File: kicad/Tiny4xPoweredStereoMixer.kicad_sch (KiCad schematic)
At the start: 23 parts, among them J1 RCJ-2221, J2 RCJ-2221, J3 RCJ-2221, J4 RCJ-2221, J5 RCJ-2221, J6 PowerConnector, J7 PowerConnector, J8 PowerConnector, U6 LM2611AMF/NOPB

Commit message: -  Fixed in-rush current problem using soft-start design. https://github.com/cracked-machine/Tiny4xPoweredStereoMixer/issues/4 - Fixed reversed pots. https://github.com/cracked-machine/Tiny4xPoweredStereoMixer/issues/3 - Made more space surrounding pwr in connector. https://github.com/cracked-machine/Tiny4xPoweredStereoMixer/issues/8
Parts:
- added C16: 100nF, Capacitor_SMD:C_0603_1608Metric_Pad1.08x0.95mm_HandSolder, symbol Device:C
- added R11: 100k, Resistor_SMD:R_0805_2012Metric_Pad1.20x1.40mm_HandSolder, symbol Device:R
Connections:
- net at C3.2, C4.2, J8.1 (Pin_1)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: now also C16.1
- net at C1.2, C15.1, J6.2 (Pin_2)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: now also R11.1; no longer U6.4 (~{SHDN})
- new net: C16.2, R11.2, U6.4 (~{SHDN})
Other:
- note added: "AUDIO PATH"
- note added: "CUK SMPS"
- moved on the sheet: C1, C15, C2, C3, C4, D1, H1, H2, H3, H4, J1, J2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

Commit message: Refactored schematic into single page (except PSU)
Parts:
- removed C1, C4: 22u, Capacitor_SMD:C_1210_3225Metric_Pad1.33x2.70mm_HandSolder, symbol Device:C
- removed C15, C16: 100nF, Capacitor_SMD:C_0603_1608Metric_Pad1.08x0.95mm_HandSolder, symbol Device:C
- removed C2: 2.2u, Capacitor_SMD:C_1210_3225Metric_Pad1.33x2.70mm_HandSolder, symbol Device:C
- removed C3: 1n, Capacitor_SMD:C_0805_2012Metric_Pad1.18x1.45mm_HandSolder, symbol Device:C
- removed D1: D_Schottky, Diode_SMD:D_PowerDI-123, symbol Device:D_Schottky
- removed J6, J7, J8: PowerConnector, Connector_PinHeader_2.54mm:PinHeader_1x02_P2.54mm_Vertical, symbol Connector:Conn_01x02_Pin
- removed L1, L2: 22u, Inductor_SMD:L_Ferrocore_DLG-0403, symbol Device:L
- removed R11: 100k, Resistor_SMD:R_0805_2012Metric_Pad1.20x1.40mm_HandSolder, symbol Device:R
- removed RFB1: 22k, Resistor_SMD:R_0805_2012Metric_Pad1.20x1.40mm_HandSolder, symbol Device:R
- removed RFB2: 2k2, Resistor_SMD:R_0805_2012Metric_Pad1.20x1.40mm_HandSolder, symbol Device:R
- removed U6: LM2611AMF/NOPB, Package_TO_SOT_SMD:SOT-23-5, symbol Regulator_Switching:LM2611xMF
- added C10, C11, C12, C13, C14, C5, C6, C7, C8, C9: 100nF, Capacitor_SMD:C_0603_1608Metric_Pad1.08x0.95mm_HandSolder, symbol Device:C
- added R1, R10, R2, R3, R4, R5, R6, R7, R8, R9: 10k, Resistor_SMD:R_0805_2012Metric_Pad1.20x1.40mm_HandSolder, symbol Device:R
- added RV1, RV2, RV3, RV4: 10k, Potentiometers:Potentiometer_Alps_RK09L_Double_Horizontal, symbol Device:R_Potentiometer_Dual_Separate
- added U1, U2, U3, U4, U5: TL072, Package_SO:SOIC-8_3.9x4.9mm_P1.27mm, symbol Amplifier_Operational:TL072
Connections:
- net +12V: now also C11.1, C13.1, C5.1, C7.1, C9.1, U1.8 (V+), U2.8 (V+), U3.8 (V+), U4.8 (V+), U5.8 (V+)
- net -12V: now also C10.1, C12.1, C14.1, C6.1, C8.1, U1.4 (V-), U2.4 (V-), U3.4 (V-), U4.4 (V-), U5.4 (V-)
- net GND: now also C10.2, C11.2, C12.2, C13.2, C14.2, C5.2, C6.2, C7.2, C8.2, C9.2, RV1.1, RV1.4, RV2.1, RV2.4, RV3.1, RV3.4, RV4.1, RV4.4, U5.3 (+), U5.5 (+)
- net BufferOpAmp1/left_channel_input: no longer names the net of J1.3 (Pin_3)
- net BufferOpAmp1/left_channel_input: now also U1.3 (+)
- net BufferOpAmp1/right_channel_input: no longer names the net of J1.2 (Pin_2)
- net BufferOpAmp1/right_channel_input: now also U1.5 (+)
- net BufferOpAmp2/left_channel_input: no longer names the net of J2.3 (Pin_3)
- net BufferOpAmp2/left_channel_input: now also U2.3 (+)
- net BufferOpAmp2/right_channel_input: no longer names the net of J2.2 (Pin_2)
- net BufferOpAmp2/right_channel_input: now also U2.5 (+)
- net BufferOpAmp3/left_channel_input: no longer names the net of J3.3 (Pin_3)
- net BufferOpAmp3/left_channel_input: now also U3.3 (+)
- net BufferOpAmp3/right_channel_input: no longer names the net of J3.2 (Pin_2)
- net BufferOpAmp3/right_channel_input: now also U3.5 (+)
- net BufferOpAmp4/left_channel_input: no longer names the net of J4.3 (Pin_3)
- net BufferOpAmp4/left_channel_input: now also U4.3 (+)
- net BufferOpAmp4/right_channel_input: no longer names the net of J4.2 (Pin_2)
- net BufferOpAmp4/right_channel_input: now also U4.5 (+)
- net MixerOpAmp/left_channel_mix_out: no longer names the net of J5.3 (Pin_3)
- net MixerOpAmp/left_channel_mix_out: now also R9.2, U5.1
- net MixerOpAmp/right_channel_mix_out: no longer names the net of J5.2 (Pin_2)
- net MixerOpAmp/right_channel_mix_out: now also R10.2, U5.7
- new net: RV3.3, U3.6 (-), U3.7
- new net: RV3.6, U3.1, U3.2 (-)
- new net: R10.1, R5.2, R6.2, R7.2, R8.2, U5.6 (-)
- new net: R1.2, R2.2, R3.2, R4.2, R9.1, U5.2 (-)
- new net: RV1.3, U1.6 (-), U1.7
- new net: RV2.3, U2.6 (-), U2.7
- new net: RV4.3, U4.6 (-), U4.7
- new net: RV1.6, U1.1, U1.2 (-)
- new net: RV4.6, U4.1, U4.2 (-)
- new net: RV2.6, U2.1, U2.2 (-)
- new net ch1_left_mix_in: R4.1, RV1.5
- new net ch1_right_mix_in: R8.1, RV1.2
- new net ch2_left_mix_in: R3.1, RV2.5
- new net ch2_right_mix_in: R7.1, RV2.2
- new net ch3_left_mix_in: R2.1, RV3.5
- new net ch3_right_mix_in: R6.1, RV3.2
- new net ch4_left_mix_in: R1.1, RV4.5
- new net ch4_right_mix_in: R5.1, RV4.2
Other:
- removed sheet BufferOpAmp1
- removed sheet BufferOpAmp2
- removed sheet BufferOpAmp3
- removed sheet BufferOpAmp4
- removed sheet MixerOpAmp
- added sheet PowerSupply (PowerSupply.kicad_sch)
- note removed: "AUDIO PATH"
- note removed: "CUK SMPS"
- moved on the sheet: H1, H2, H3, H4, J1, J5

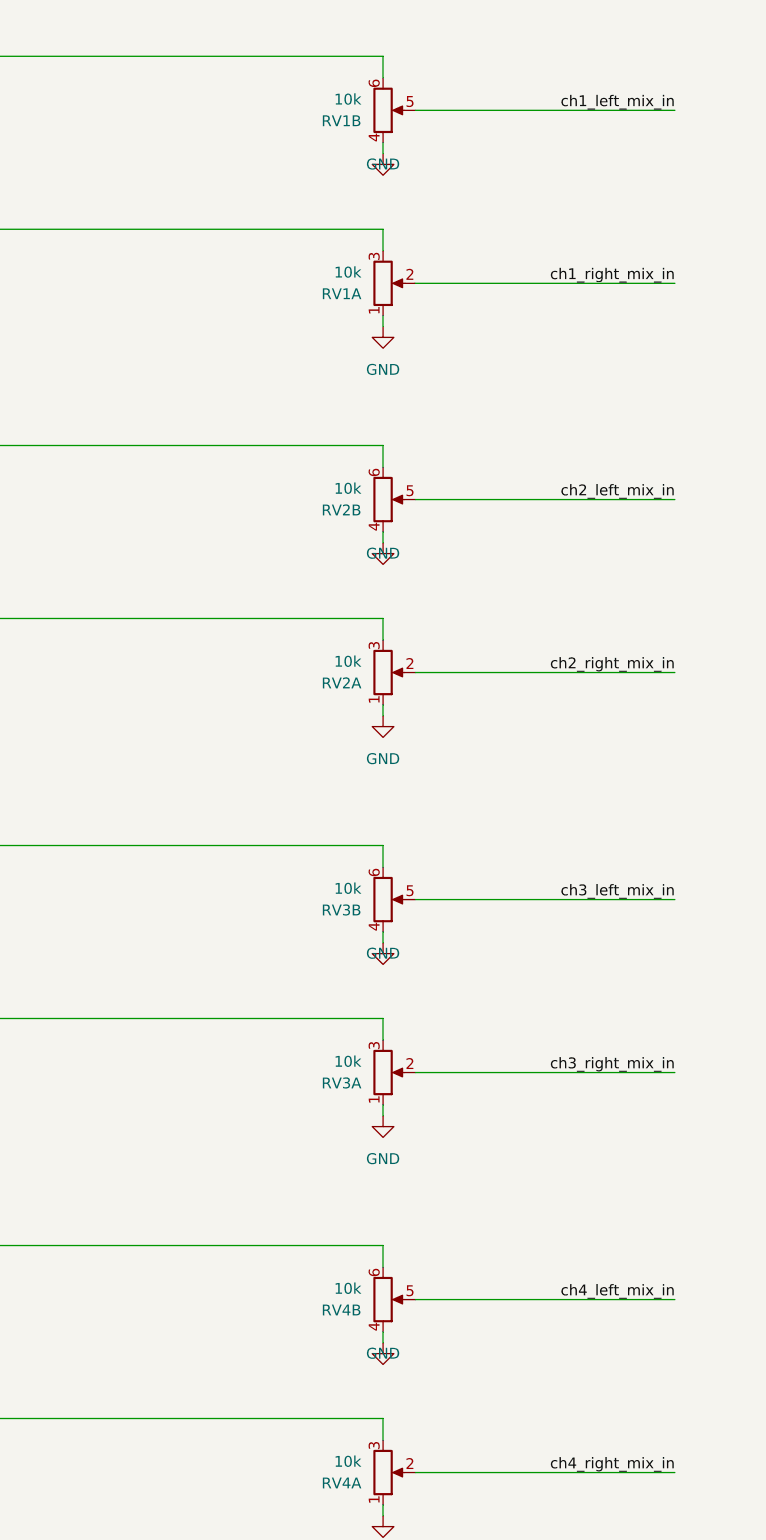
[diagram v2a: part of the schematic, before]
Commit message: - updated pots to rk12l12
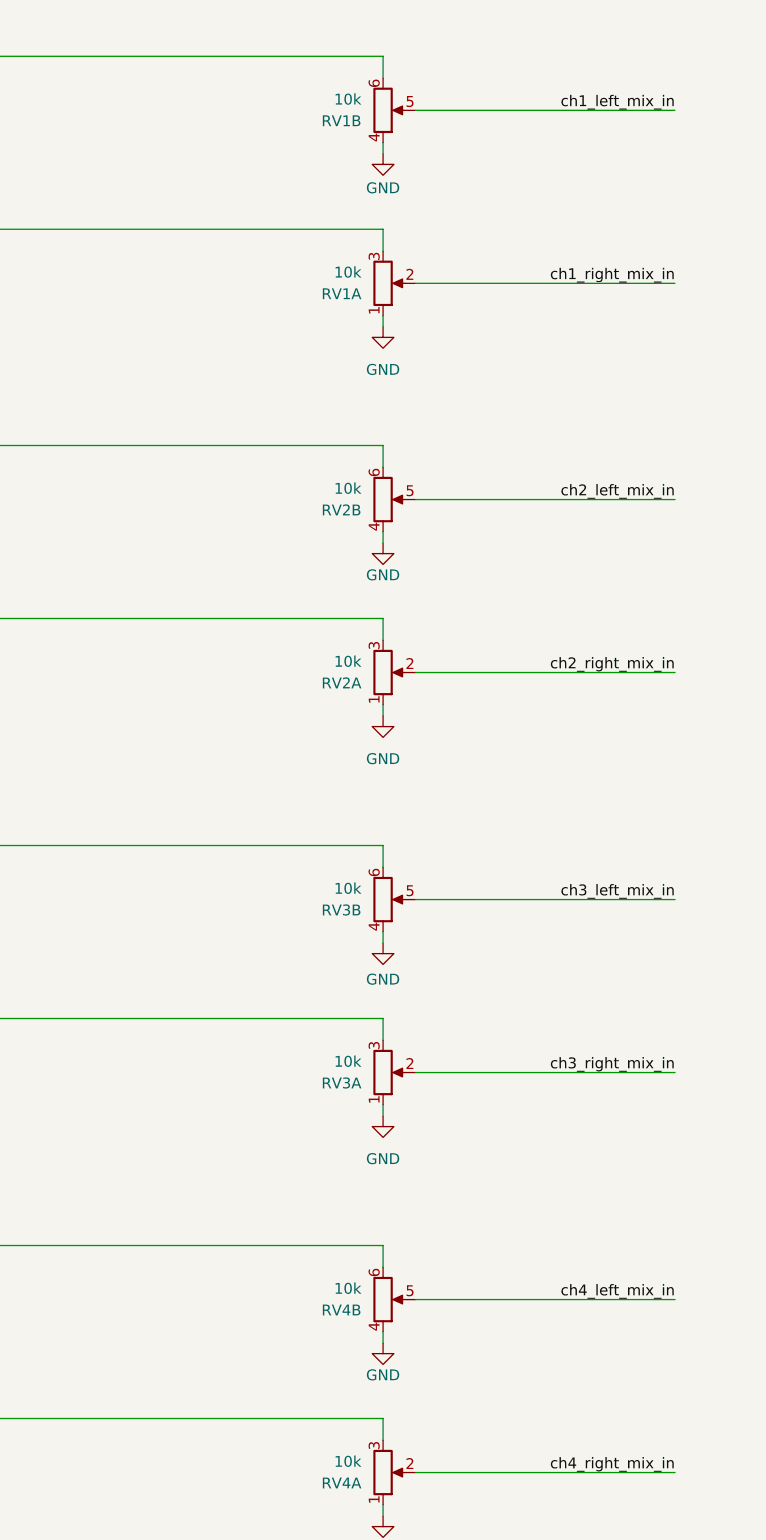
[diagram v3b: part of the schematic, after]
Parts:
- RV1, RV2, RV3, RV4: footprint Potentiometers:Potentiometer_Alps_RK09L_Double_Horizontal -> Potentiometers:Alps_RK12L12_Double_Horizontal; Mouser 688-RK09L12B0A4S -> 688-RK12L1210C1K
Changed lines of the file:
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@@
 			)
 		)
-		(property "Footprint" "Potentiometers:Potentiometer_Alps_RK09L_Double_Horizontal"
+		(property "Footprint" "Potentiometers:Alps_RK12L12_Double_Horizontal"
 			(at 160.02 57.15 0)
 			(effects
@@
 			)
 		)
-		(property "Datasheet" "~"
+		(property "Datasheet" "https://www.mouser.co.uk/datasheet/2/15/RK12L12_VARIETYOTHER-1370614.pdf"
 			(at 160.02 57.15 0)
 			(effects
@@
 			)
 		)
-		(property "Description" "Dual potentiometer, separate units"
+		(property "Description" "Dual potentiometer, separate units, linear taper"
 			(at 160.02 57.15 0)
 			(effects
@@
 			)
 		)
-		(property "Mouser" "688-RK09L12B0A4S "
+		(property "Mouser" "688-RK12L1210C1K "
 			(at 160.02 57.15 0)
 			(effects
@@
 			)
 		)
-		(property "Footprint" "Potentiometers:Potentiometer_Alps_RK09L_Double_Horizontal"
+		(property "Footprint" "Potentiometers:Alps_RK12L12_Double_Horizontal"
 			(at 160.02 102.87 0)
 			(effects
@@
 			)
 		)
-		(property "Datasheet" "~"
+		(property "Datasheet" "https://www.mouser.co.uk/datasheet/2/15/RK12L12_VARIETYOTHER-1370614.pdf"
 			(at 160.02 102.87 0)
 			(effects
@@
 			)
 		)
-		(property "Description" "Dual potentiometer, separate units"
+		(property "Description" "Dual potentiometer, separate units, linear taper"
 			(at 160.02 102.87 0)
 			(effects
@@
 			)
 		)
-		(property "Mouser" "688-RK09L12B0A4S "
+		(property "Mouser" "688-RK12L1210C1K "
 			(at 160.02 102.87 0)
 			(effects
@@
 			)
 		)
-		(property "Datasheet" "~"
+		(property "Datasheet" "https://www.mouser.co.uk/datasheet/2/670/rcj_22-3159382.pdf"
 			(at 41.91 132.08 0)
 			(effects
@@
 			)
 		)
-		(property "Footprint" "Potentiometers:Potentiometer_Alps_RK09L_Double_Horizontal"
+		(property "Footprint" "Potentiometers:Alps_RK12L12_Double_Horizontal"
 			(at 160.02 196.85 0)
 			(effects
@@
 			)
 		)
-		(property "Datasheet" "~"
+		(property "Datasheet" "https://www.mouser.co.uk/datasheet/2/15/RK12L12_VARIETYOTHER-1370614.pdf"
 			(at 160.02 196.85 0)
 			(effects
@@
 			)
 		)
-		(property "Description" "Dual potentiometer, separate units"
+		(property "Description" "Dual potentiometer, separate units, linear taper"
 			(at 160.02 196.85 0)
 			(effects
@@
 			)
 		)
-		(property "Mouser" "688-RK09L12B0A4S "
+		(property "Mouser" "688-RK12L1210C1K "
 			(at 160.02 196.85 0)
 			(effects
@@
 			)
 		)
-		(property "Footprint" "Potentiometers:Potentiometer_Alps_RK09L_Double_Horizontal"
+		(property "Footprint" "Potentiometers:Alps_RK12L12_Double_Horizontal"
 			(at 160.02 36.83 0)
 			(effects
@@
 			)
 		)
-		(property "Datasheet" "~"
+		(property "Datasheet" "https://www.mouser.co.uk/datasheet/2/15/RK12L12_VARIETYOTHER-1370614.pdf"
 			(at 160.02 36.83 0)
 			(effects
@@
 			)
 		)
-		(property "Description" "Dual potentiometer, separate units"
+		(property "Description" "Dual potentiometer, separate units, linear taper"
 			(at 160.02 36.83 0)
 			(effects
@@
 			)
 		)
-		(property "Mouser" "688-RK09L12B0A4S "
+		(property "Mouser" "688-RK12L1210C1K "
 			(at 160.02 36.83 0)
 			(effects
@@
 		)
 		(property "Value" "GND"
-			(at 160.02 88.9 0)
+			(at 160.02 91.44 0)
 			(effects
 				(font
@@
 			)
 		)
-		(property "Footprint" "Potentiometers:Potentiometer_Alps_RK09L_Double_Horizontal"
+		(property "Footprint" "Potentiometers:Alps_RK12L12_Double_Horizontal"
 			(at 160.02 176.53 0)
 			(effects
@@
 			)
 		)
-		(property "Datasheet" "~"
+		(property "Datasheet" "https://www.mouser.co.uk/datasheet/2/15/RK12L12_VARIETYOTHER-1370614.pdf"
 			(at 160.02 176.53 0)
 			(effects
@@
 			)
 		)
-		(property "Description" "Dual potentiometer, separate units"
+		(property "Description" "Dual potentiometer, separate units, linear taper"
 			(at 160.02 176.53 0)
 			(effects
@@
 			)
 		)
-		(property "Mouser" "688-RK09L12B0A4S "
+		(property "Mouser" "688-RK12L1210C1K "
 			(at 160.02 176.53 0)
 			(effects
@@
 		)
 		(property "Value" "GND"
-			(at 160.02 43.18 0)
+			(at 160.02 45.974 0)
 			(effects
 				(font
@@
 			)
 		)
-		(property "Footprint" "Potentiometers:Potentiometer_Alps_RK09L_Double_Horizontal"
+		(property "Footprint" "Potentiometers:Alps_RK12L12_Double_Horizontal"
 			(at 160.02 149.86 0)
 			(effects
@@
 			)
 		)
-		(property "Datasheet" "~"
+		(property "Datasheet" "https://www.mouser.co.uk/datasheet/2/15/RK12L12_VARIETYOTHER-1370614.pdf"
 			(at 160.02 149.86 0)
 			(effects
@@
 			)
 		)
-		(property "Description" "Dual potentiometer, separate units"
+		(property "Description" "Dual potentiometer, separate units, linear taper"
 			(at 160.02 149.86 0)
 			(effects
@@
 			)
 		)
-		(property "Mouser" "688-RK09L12B0A4S "
+		(property "Mouser" "688-RK12L1210C1K "
 			(at 160.02 149.86 0)
 			(effects
@@
 			)
 		)
-		(property "Footprint" "Potentiometers:Potentiometer_Alps_RK09L_Double_Horizontal"
+		(property "Footprint" "Potentiometers:Alps_RK12L12_Double_Horizontal"
 			(at 160.02 129.54 0)
 			(effects
@@
 			)
 		)
-		(property "Datasheet" "~"
+		(property "Datasheet" "https://www.mouser.co.uk/datasheet/2/15/RK12L12_VARIETYOTHER-1370614.pdf"
 			(at 160.02 129.54 0)
 			(effects
@@
 			)
 		)
-		(property "Description" "Dual potentiometer, separate units"
+		(property "Description" "Dual potentiometer, separate units, linear taper"
 			(at 160.02 129.54 0)
 			(effects
@@
 			)
 		)
-		(property "Mouser" "688-RK09L12B0A4S "
+		(property "Mouser" "688-RK12L1210C1K "
 			(at 160.02 129.54 0)
 			(effects
@@
 			)
 		)
-		(property "Footprint" "Potentiometers:Potentiometer_Alps_RK09L_Double_Horizontal"
+		(property "Footprint" "Potentiometers:Alps_RK12L12_Double_Horizontal"
 			(at 160.02 82.55 0)
 			(effects
@@
 			)
 		)
-		(property "Datasheet" "~"
+		(property "Datasheet" "https://www.mouser.co.uk/datasheet/2/15/RK12L12_VARIETYOTHER-1370614.pdf"
 			(at 160.02 82.55 0)
 			(effects
@@
 			)
 		)
-		(property "Description" "Dual potentiometer, separate units"
+		(property "Description" "Dual potentiometer, separate units, linear taper"
 			(at 160.02 82.55 0)
 			(effects
@@
 			)
 		)
-		(property "Mouser" "688-RK09L12B0A4S "
+		(property "Mouser" "688-RK12L1210C1K "
 			(at 160.02 82.55 0)
 			(effects
@@
 			)
 		)
-		(property "Datasheet" "~"
+		(property "Datasheet" "https://www.mouser.co.uk/datasheet/2/670/rcj_22-3159382.pdf"
 			(at 388.62 146.05 0)
 			(effects
@@
 			)
 		)
-		(property "Datasheet" "~"
+		(property "Datasheet" "https://www.mouser.co.uk/datasheet/2/670/rcj_22-3159382.pdf"
 			(at 41.91 85.09 0)
 			(effects
@@
 			)
 		)
-		(property "Datasheet" "~"
+		(property "Datasheet" "https://www.mouser.co.uk/datasheet/2/670/rcj_22-3159382.pdf"
 			(at 41.91 39.37 0)
 			(effects
@@
 			)
 		)
-		(property "Datasheet" "~"
+		(property "Datasheet" "https://www.mouser.co.uk/datasheet/2/670/rcj_22-3159382.pdf"
 			(at 41.91 179.07 0)
 			(effects
@@
 		)
 		(property "Value" "GND"
-			(at 160.02 135.89 0)
+			(at 160.02 138.938 0)
 			(effects
 				(font
@@
 		)
 		(property "Value" "GND"
-			(at 160.02 182.88 0)
+			(at 160.02 185.42 0)
 			(effects
 				(font

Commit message: replaced phono connectors with 3.5mm stereo jack connectors so that unplugged connections are switched to ground
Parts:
- removed H3, H4: MountingHole, MountingHole:MountingHole_3mm, symbol Mechanical:MountingHole
- removed J1, J2, J3, J4, J5: RCJ-2221, RCAJack:CUI_DEVICES_RCJ-2211, symbol Connector:Conn_01x03_Pin
- removed unit 1 of U1
- removed unit 2 of U1
- removed U3, U4: TL072, Package_SO:SOIC-8_3.9x4.9mm_P1.27mm, symbol Amplifier_Operational:TL072
- removed unit 3 of U5
- added C17, C18: 100nF, Capacitor_SMD:C_0603_1608Metric_Pad1.08x0.95mm_HandSolder, symbol Device:C
- added C19, C20: 10uF, Capacitor_SMD:C_1210_3225Metric_Pad1.33x2.70mm_HandSolder, symbol Device:C
- added J1, J2, J3, J4, J9: AudioJack3_SwitchTR, Connector_Audio:Jack_3.5mm_CUI_SJ1-3535NG_Horizontal, symbol Connector_Audio:AudioJack3_SwitchTR
- added R12, R13, R14, R15: 10k, Resistor_SMD:R_0805_2012Metric_Pad1.20x1.40mm_HandSolder, symbol Device:R
- renumbered U5 to U1
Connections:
- net +12V: no longer C11.1, C5.1, C7.1
- net -12V: no longer C10.1, C12.1, C14.1
- net GND: now also U2.3 (+), U2.5 (+), J1.RN, J1.S, J1.TN, J2.RN, J2.S, J2.TN, J3.RN, J3.S, J3.TN, J4.RN, J4.S, J4.TN, J9.RN, J9.S, J9.TN; no longer C10.2, C11.2, C12.2, C14.2, C5.2, C7.2
- net at RV3.3: now also C14.2
- net at RV3.6: now also C12.2
- net at R5.2, R6.2, R7.2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: now also R9.1, U1.2 (-); no longer R10.1, U1.6 (-)
- net at R10.2, U1.7: now also C20.1
- net at R1.2, R2.2, R3.2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: now also U2.2 (-), R13.1; no longer R9.1, U1.2 (-)
- net at RV1.3: now also C7.2
- net at R9.2, U1.1: now also R12.1
- net at RV4.3: now also C18.2
- net at RV1.6: now also C5.2
- net at RV4.6: now also C17.2
- new net: C10.1, J2.T
- new net: C10.2, RV2.6
- new net: R10.1, R12.2, U1.6 (-)
- new net: R13.2, R14.1, U2.1
- new net: R14.2, R15.1, U2.6 (-)
- new net: C18.1, J4.R
- new net: C17.1, J4.T
- new net: C19.1, R15.2, U2.7
- new net: C19.2, J9.T
- new net: C11.2, RV2.3
- new net: C7.1, J1.R
- new net: C12.1, J3.T
- new net: C14.1, J3.R
- new net: C20.2, J9.R
- new net: C5.1, J1.T
- new net: C11.1, J2.R
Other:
- moved on the sheet: R1, R10, R2, R3, R4, R5, R6, R7, R8, R9, RV1A, RV1B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

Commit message: completed revb layout
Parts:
- added TP1: TestPoint, TestPoint:TestPoint_Keystone_5005-5009_Compact, symbol Connector:TestPoint
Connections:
- net GND: now also TP1.1
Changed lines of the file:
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@@
 	(wire
 		(pts
+			(xy 83.82 256.54) (xy 83.82 260.35)
+		)
+		(stroke
+			(width 0)
+			(type default)
+		)
+	)
+	(wire
+		(pts
 			(xy 104.14 151.13) (xy 104.14 152.4)
 		)
@@
 	)
 	(symbol
+		(lib_id "power:GND")
+		(at 83.82 260.35 0)
+		(unit 1)
+		(exclude_from_sim no)
+		(in_bom yes)
+		(on_board yes)
+		(dnp no)
+		(fields_autoplaced yes)
+		(property "Reference" "#PWR08"
+			(at 83.82 266.7 0)
+			(effects
+				(font
+					(size 1.27 1.27)
+				)
+				(hide yes)
+			)
+		)
+		(property "Value" "GND"
+			(at 83.82 265.43 0)
+			(effects
+				(font
+					(size 1.27 1.27)
+				)
+			)
+		)
+		(property "Footprint" ""
+			(at 83.82 260.35 0)
+			(effects
+				(font
+					(size 1.27 1.27)
+				)
+				(hide yes)
+			)
+		)
+		(property "Datasheet" ""
+			(at 83.82 260.35 0)
+			(effects
+				(font
+					(size 1.27 1.27)
+				)
+				(hide yes)
+			)
+		)
+		(property "Description" "Power symbol creates a global label with name \"GND\" , ground"
+			(at 83.82 260.35 0)
+			(effects
+				(font
+					(size 1.27 1.27)
+				)
+				(hide yes)
+			)
+		)
+		(pin "1"
+		)
+		(instances
+			(project "Tiny4xPoweredStereoMixer"
+				(path "/68c4b081-ef47-4ba5-a55f-4ef66cb2b598"
+					(reference "#PWR08")
+					(unit 1)
+				)
+			)
+		)
+	)
+	(symbol
 		(lib_id "Device:C")
 		(at 148.59 252.73 0)
@@
 	)
 	(symbol
+		(lib_id "Connector:TestPoint")
+		(at 83.82 256.54 0)
+		(unit 1)
+		(exclude_from_sim no)
+		(in_bom yes)
+		(on_board yes)
+		(dnp no)
+		(fields_autoplaced yes)
+		(property "Reference" "TP1"
+			(at 86.36 251.9679 0)
+			(effects
+				(font
+					(size 1.27 1.27)
+				)
+				(justify left)
+			)
+		)
+		(property "Value" "TestPoint"
+			(at 86.36 254.5079 0)
+			(effects
+				(font
+					(size 1.27 1.27)
+				)
+				(justify left)
+			)
+		)
+		(property "Footprint" "TestPoint:TestPoint_Keystone_5005-5009_Compact"
+			(at 88.9 256.54 0)
+			(effects
+				(font
+					(size 1.27 1.27)
+				)
+				(hide yes)
+			)
+		)
+		(property "Datasheet" "https://www.mouser.co.uk/datasheet/2/215/5005_5009-743680.pdf"
+			(at 88.9 256.54 0)
+			(effects
+				(font
+					(size 1.27 1.27)
+				)
+				(hide yes)
+			)
+		)
+		(property "Description" "test point"
+			(at 83.82 256.54 0)
+			(effects
+				(font
+					(size 1.27 1.27)
+				)
+				(hide yes)
+			)
+		)
+		(property "Mouser" "534-5006"
+			(at 83.82 256.54 0)
+			(effects
+				(font
+					(size 1.27 1.27)
+				)
+				(hide yes)
+			)
+		)
+		(pin "1"
+		)
+		(instances
+			(project "Tiny4xPoweredStereoMixer"
+				(path "/68c4b081-ef47-4ba5-a55f-4ef66cb2b598"
+					(reference "TP1")
+					(unit 1)
+				)
+			)
+		)
+	)
+	(symbol
 		(lib_id "power:-12V")
 		(at 158.75 242.57 0)
@@
 	)
 	(sheet
-		(at 307.34 218.44)
+		(at 295.91 201.93)
 		(size 63.5 29.21)
 		(fields_autoplaced yes)
@@
 		)
 		(property "Sheetname" "PowerSupply"
-			(at 307.34 217.7284 0)
+			(at 295.91 201.2184 0)
 			(effects
 				(font
@@
 		)
 		(property "Sheetfile" "PowerSupply.kicad_sch"
-			(at 307.34 248.2346 0)
+			(at 295.91 231.7246 0)
 			(effects
 				(font
